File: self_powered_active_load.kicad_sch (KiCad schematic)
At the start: 90 parts, among them J1 Conn_01x05, J2 Conn_01x03, J3 BANANA_CONN, J4 BANANA_CONN, Q1 2SC4117, Q2 BDW94CFP, Q3 MMBT5401, Q5 MMBT5401, Q6 MMBT5401, U1 LM10CWM

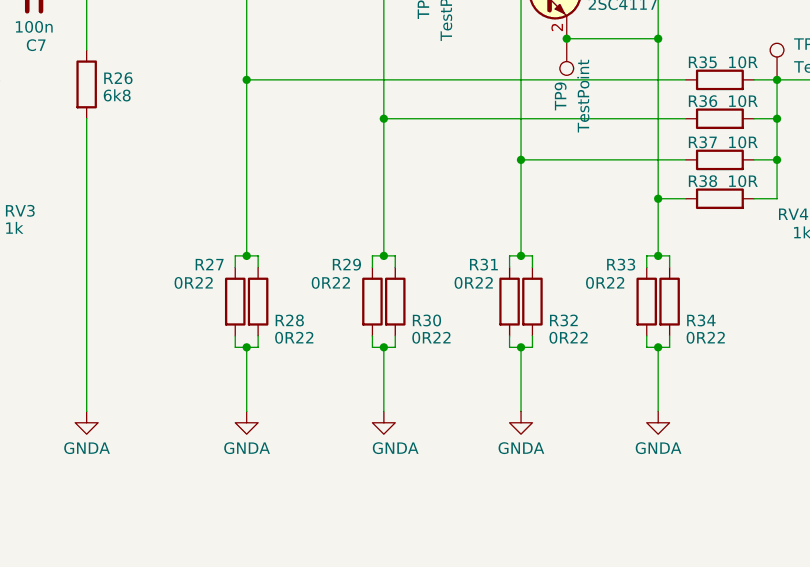
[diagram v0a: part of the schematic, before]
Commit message: error fixed shunts
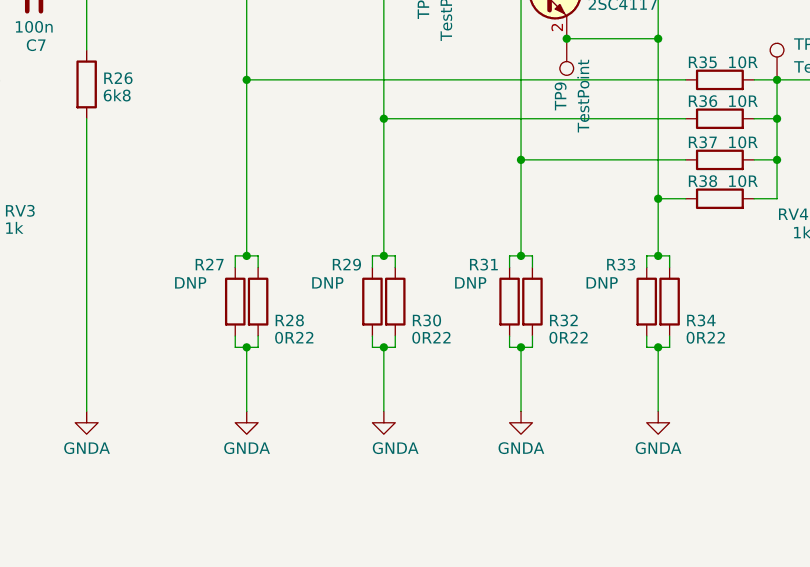
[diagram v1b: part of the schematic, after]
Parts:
- R27, R29, R31, R33: value 0R22 -> DNP
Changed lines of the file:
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@@
       (effects (font (size 1.27 1.27)) (justify left))
     )
-    (property "Value" "0R22" (at 235.204 123.698 0)
+    (property "Value" "DNP" (at 235.204 123.698 0)
       (effects (font (size 1.27 1.27)) (justify left))
     )
@@
       (effects (font (size 1.27 1.27)) (justify left))
     )
-    (property "Value" "0R22" (at 189.484 123.698 0)
+    (property "Value" "DNP" (at 189.484 123.698 0)
       (effects (font (size 1.27 1.27)) (justify left))
     )
@@
       (effects (font (size 1.27 1.27)) (justify left))
     )
-    (property "Value" "0R22" (at 220.599 123.698 0)
+    (property "Value" "DNP" (at 220.599 123.698 0)
       (effects (font (size 1.27 1.27)) (justify left))
     )
@@
       (effects (font (size 1.27 1.27)) (justify left))
     )
-    (property "Value" "0R22" (at 204.724 123.698 0)
-      (effects (font (size 1.27 1.27)) (justify left))
-    )
+    (property "Value" "DNP" (at 204.724 123.698 0)
+      (effects (font (size 1.27 1.27)) (justify left))
+    )

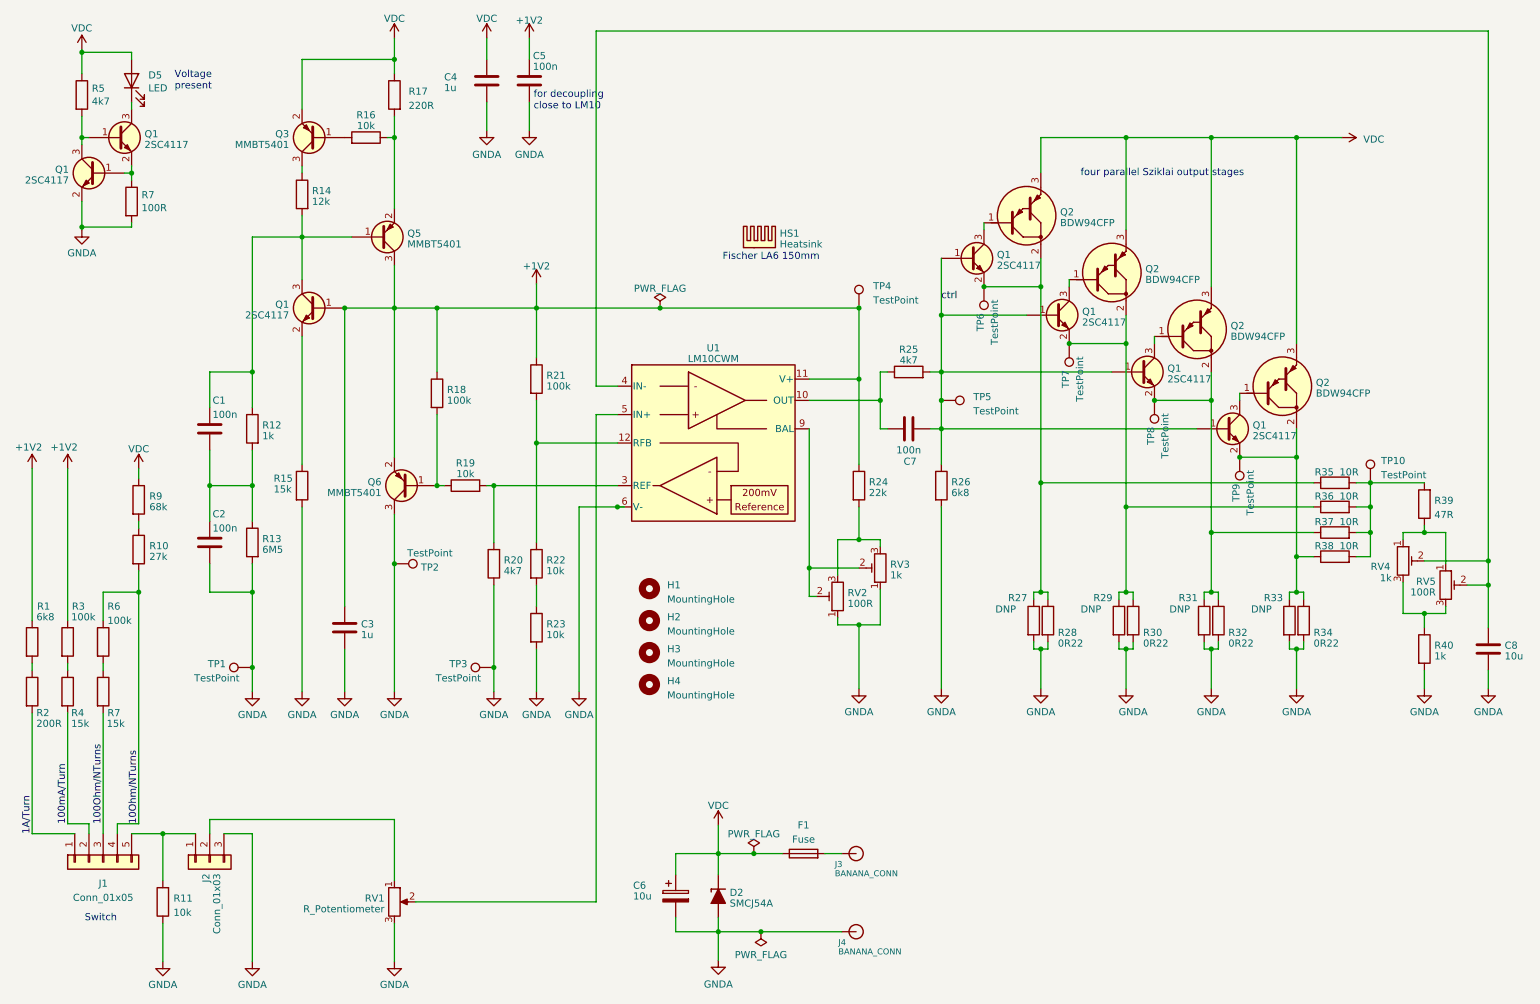
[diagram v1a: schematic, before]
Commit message: error removed shunt in PCB
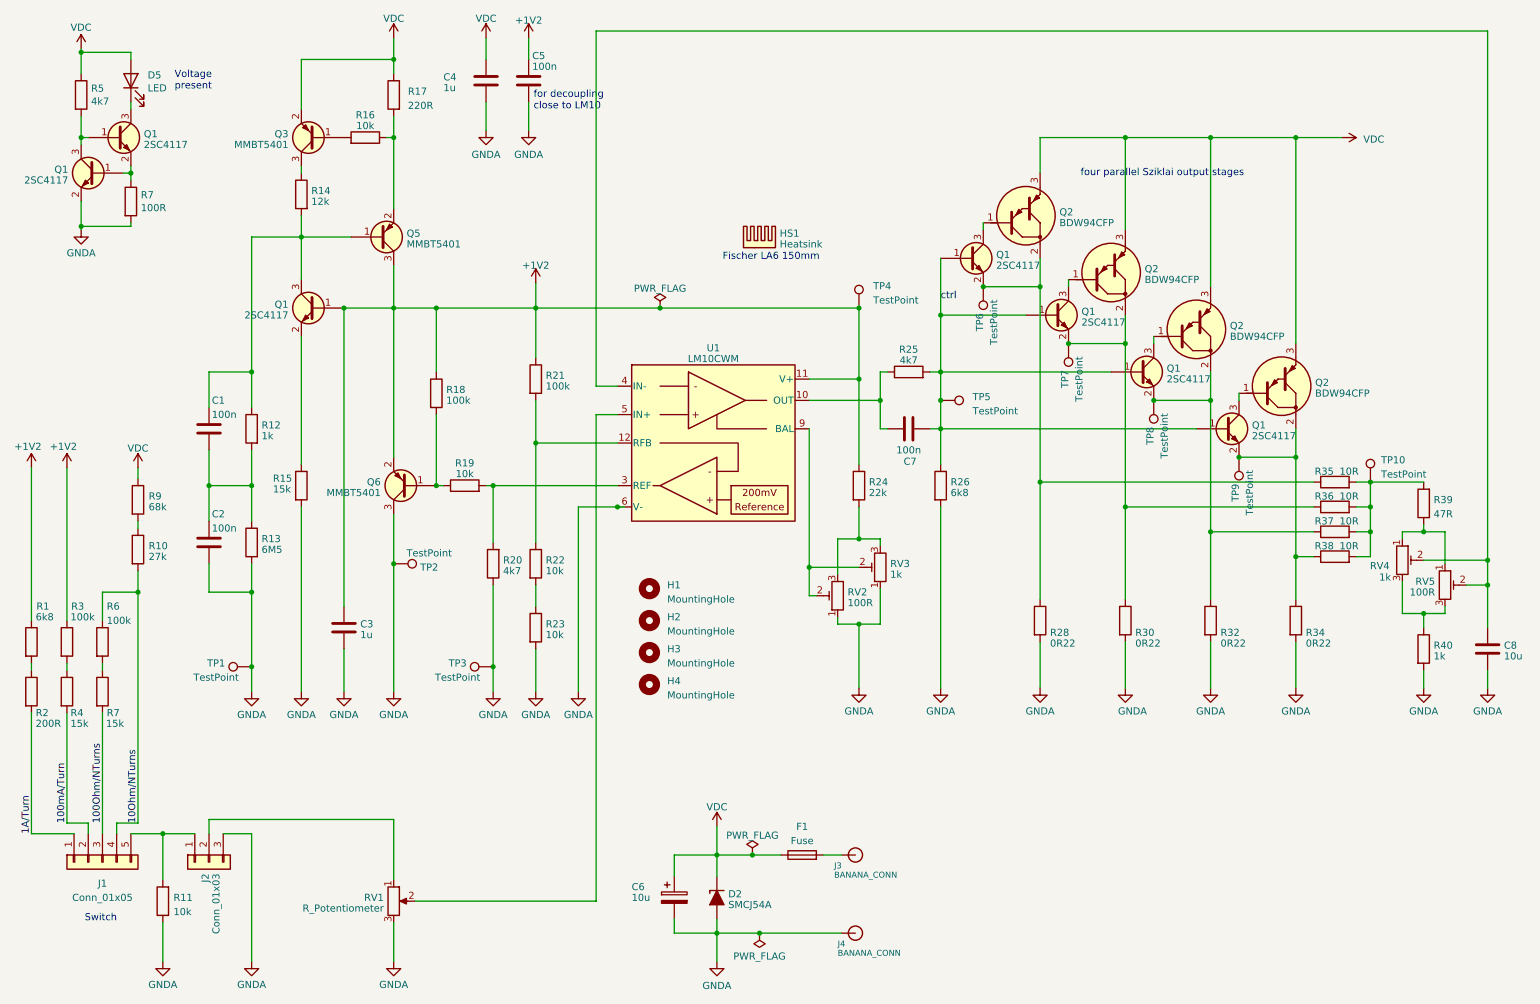
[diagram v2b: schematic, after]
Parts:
- removed R27, R29, R31, R33: DNP, Resistor_THT:R_Axial_DIN0922_L20.0mm_D9.0mm_P30.48mm_Horizontal, symbol Device:R
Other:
- moved on the sheet: R28, R30, R32, R34
